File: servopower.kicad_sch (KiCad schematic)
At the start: 18 parts, among them IC1 SIC437DED-T1-GE3

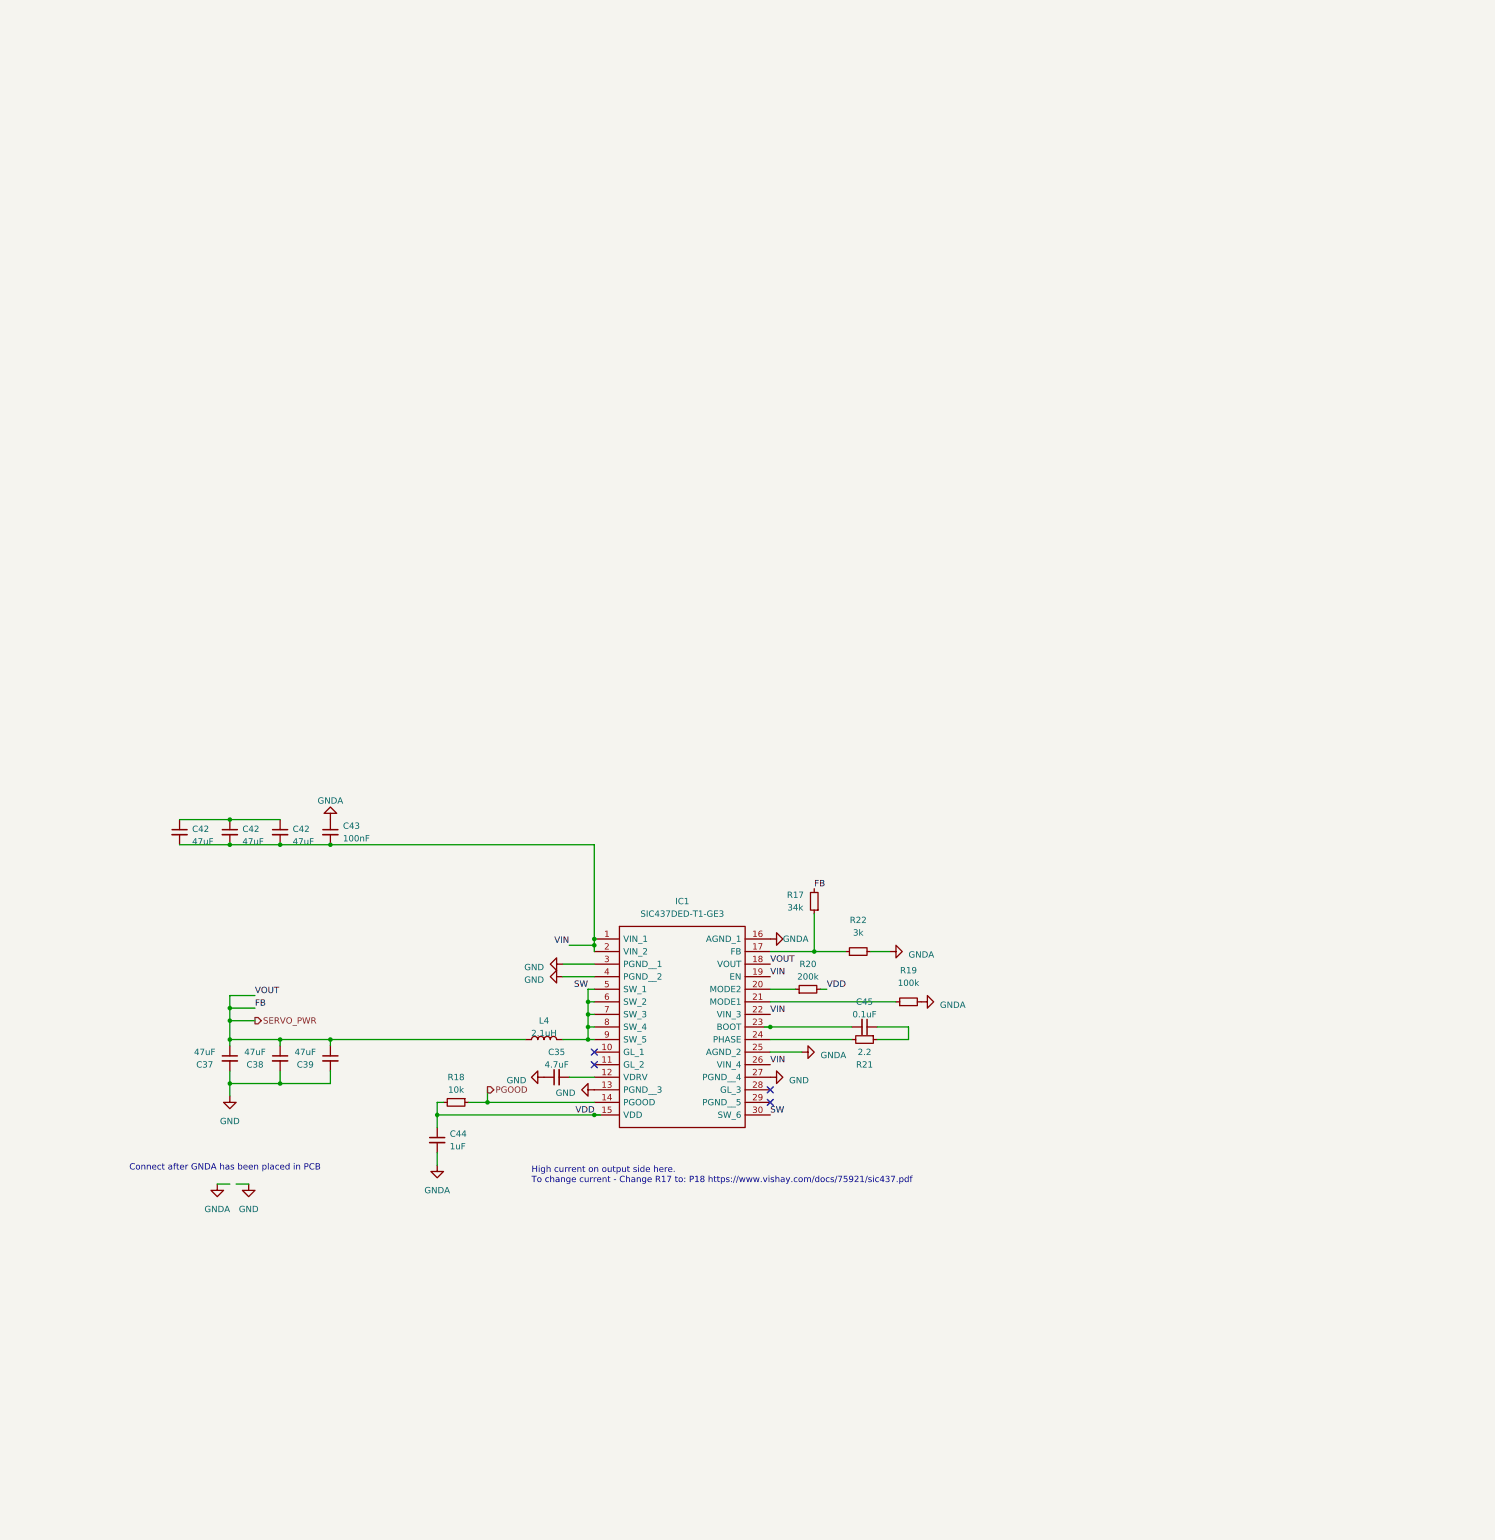
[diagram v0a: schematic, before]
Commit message: error encountered - battery logic and inductor
- use large capacitor?
- use VBUS as a power source?
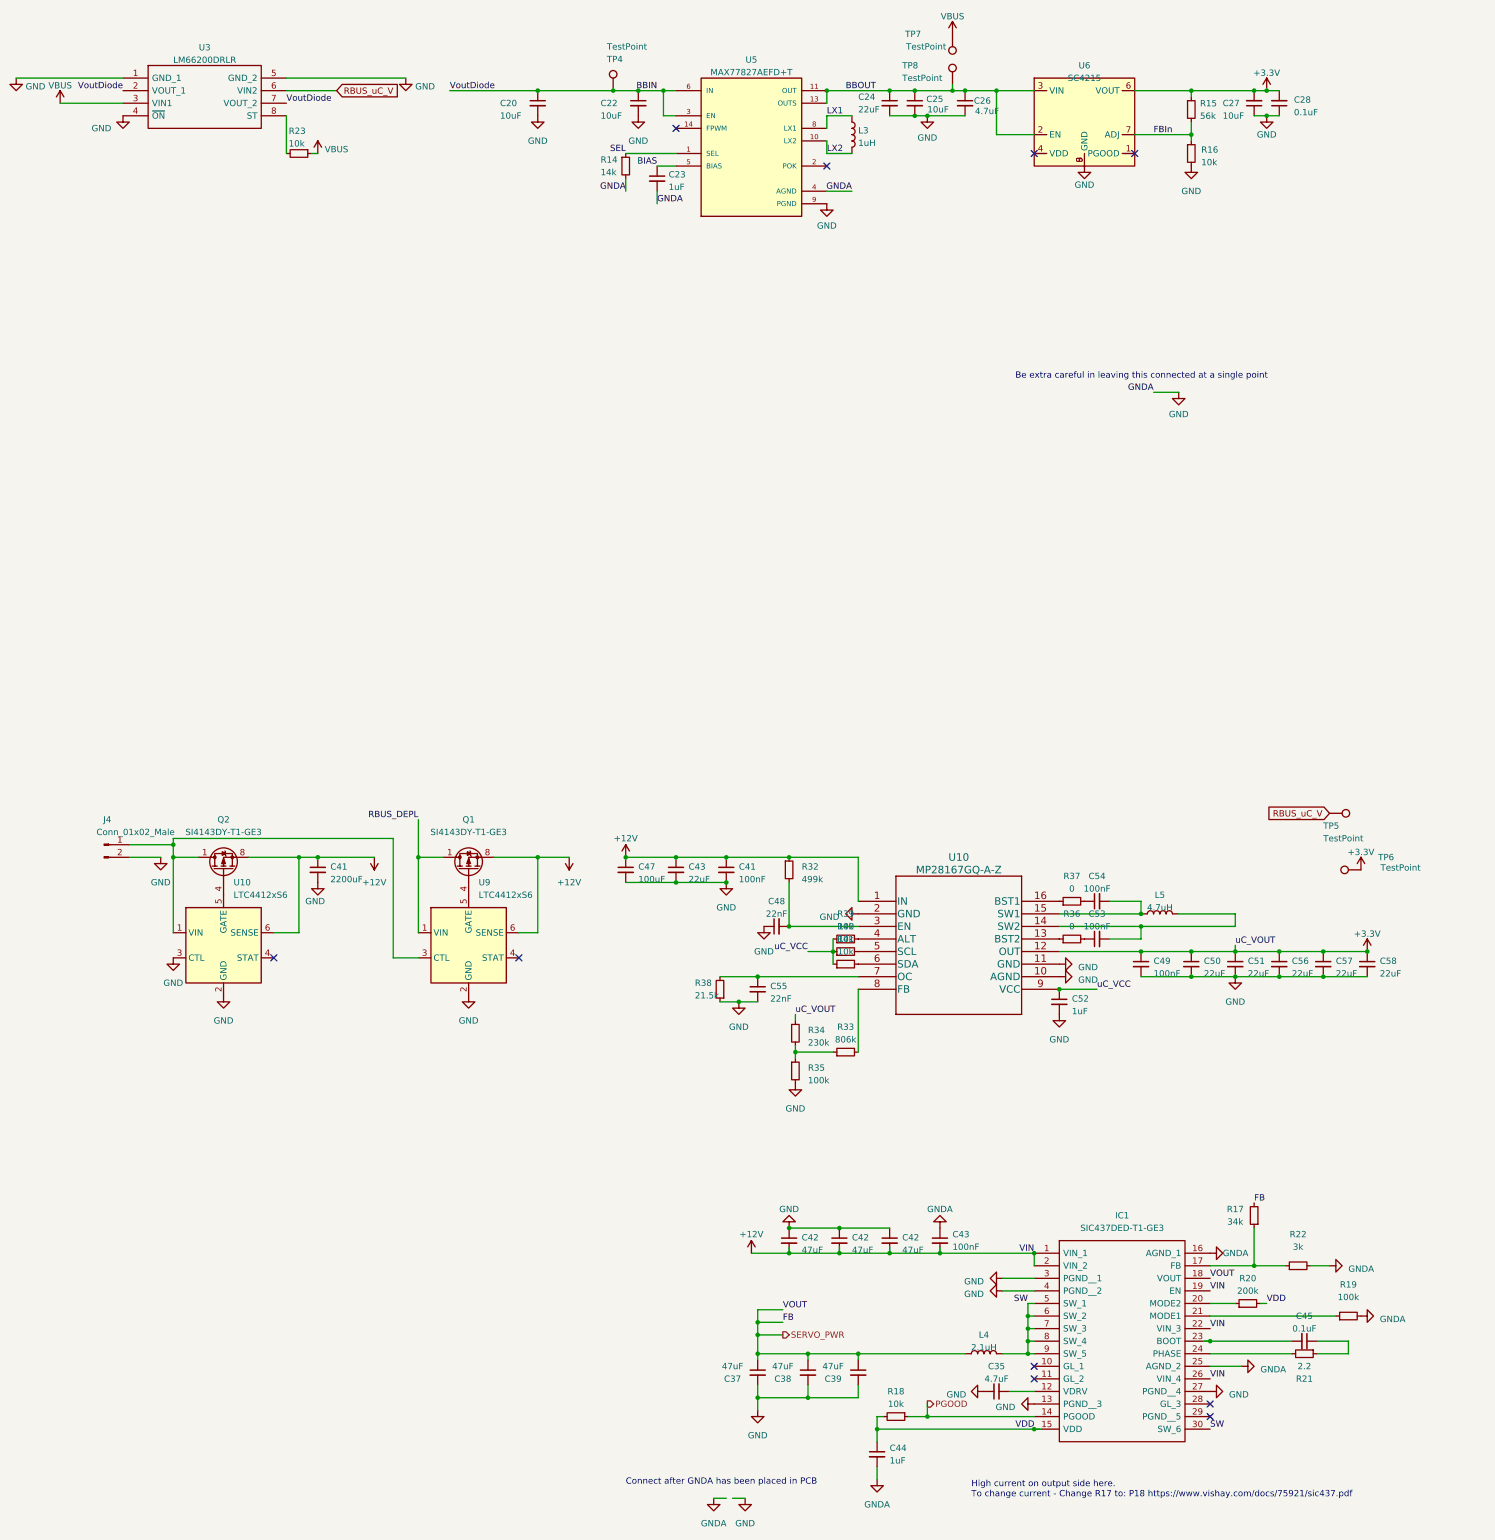
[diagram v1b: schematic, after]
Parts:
- added C20, C25, C27: 10uF, Capacitor_SMD:C_0402_1005Metric, symbol Device:C_Small
- added C22: 10uF, Capacitor_SMD:C_0603_1608Metric, symbol Device:C_Small
- added C23: 1uF, Capacitor_SMD:C_0402_1005Metric, symbol Device:C_Small
- added C24: 22uF, Capacitor_SMD:C_0603_1608Metric, symbol Device:C_Small
- added C26: 4.7uF, Capacitor_SMD:C_0402_1005Metric, symbol Device:C_Small
- added C28: 0.1uF, Capacitor_SMD:C_0402_1005Metric, symbol Device:C_Small
- added C41, C49, C53, C54: 100nF, symbol Device:C_Small
- added C41: 2200uF, Capacitor_SMD:CP_Elec_16x17.5, symbol Device:C_Small
- added C43, C50, C51, C56, C57, C58: 22uF, symbol Device:C_Small
- added C47: 100uF, symbol Device:C_Small
- added C48, C55: 22nF, symbol Device:C_Small
- added C52: 1uF, symbol Device:C_Small
- added J4: Conn_01x02_Male, iclr:AMASS_XT60PW-F, symbol Connector:Conn_01x02_Male
- added L3: 1uH, Inductor_SMD:L_0805_2012Metric, symbol Device:L
- added L5: 4.7uH, symbol Device:L
- added Q1, Q2: SI4143DY-T1-GE3, Package_SO:SOIC-8_3.9x4.9mm_P1.27mm, symbol Device:Q_PMOS_GDS
- added R14: 14k, Resistor_SMD:R_0402_1005Metric, symbol Device:R_Small
- added R15: 56k, Resistor_SMD:R_0402_1005Metric, symbol Device:R_Small
- added R16, R23: 10k, Resistor_SMD:R_0402_1005Metric, symbol Device:R_Small
- added R32: 499k, symbol Device:R_Small
- added R33: 806k, symbol Device:R_Small
- added R34: 230k, symbol Device:R_Small
- added R35: 100k, symbol Device:R_Small
- added R36, R37: 0, symbol Device:R_Small
- added R38: 21.5k, symbol Device:R_Small
- added R39, R40, R41: 10k, symbol Device:R_Small
- added TP4, TP5, TP6, TP7, TP8: TestPoint, TestPoint:TestPoint_Pad_D1.5mm, symbol Connector:TestPoint
- added U10, U9: LTC4412xS6, Package_TO_SOT_SMD:TSOT-23-6, symbol Power_Management:LTC4412xS6
- added U10: MP28167GQ-A-Z, QFN-16_MP28167_MNP, symbol iclr:MP28167GQ-A-Z
- added U3: LM66200DRLR, iclr:SOTFL50P160X60-8N, symbol iclr:LM66200DRLR
- added U5: MAX77827AEFD+T, iclr:CONV_MAX77827AEFD+T, symbol iclr:MAX77827AEFD+T
- added U6: SC4215, iclr:SOIC127P599X175-9N, symbol iclr:RT9025-25GSP
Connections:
- net GNDA is gone; now on net GND: C43.1, C44.2, IC1.16 (AGND_1), IC1.25 (AGND_2), R19.2, R22.2
- net GND: now also C42.1, C42.1, C42.1, C20.2, C22.2, C23.2, C24.2, C25.2, C26.2, C27.1, C28.1, C41.2, C41.2, C43.2, C47.2, C48.1, C49.2, C50.2, C51.2, C52.2, C55.2, C56.2, C57.2, C58.2, J4.2 (Pin_2), R14.2, R16.2, R35.2, R38.1, U10.10 (AGND), U10.11 (GND), U10.2 (GND), U10.2 (GND), U10.3 (CTL), U3.1 (GND_1), U3.4 (~{ON}), U3.5 (GND_2), U5.4 (AGND), U5.9 (PGND), U6.8 (GND), U6.9 (GND), U9.2 (GND)
- net VIN renamed +12V
- net +12V: now also C41.1, C41.1, C43.1, C47.1, Q1.5 (D), Q1.6 (D), Q1.7 (D), Q1.8 (D), Q2.5 (D), Q2.6 (D), Q2.7 (D), Q2.8 (D), R32.1, U10.1 (IN), U10.6 (SENSE), U9.6 (SENSE)
- new net: C53.1, R36.2
- new net: C53.2, L5.2, U10.14 (SW2)
- new net: J4.1 (Pin_1), Q2.1 (S), Q2.2 (S), Q2.3 (S), U10.1 (VIN), U9.3 (CTL)
- new net: Q2.4 (G), U10.5 (GATE)
- new net: C54.1, R37.2
- new net: C54.2, L5.1, U10.15 (SW1)
- new net: Q1.4 (G), U9.5 (GATE)
- new net: C48.2, R32.2, U10.3 (EN)
- new net: R33.1, R34.2, R35.1
- new net: R33.2, U10.8 (FB)
- new net: R40.2, U10.5 (SCL)
- new net: R36.1, U10.13 (BST2)
- new net: C55.1, R38.2, U10.7 (OC)
- new net: R37.1, U10.16 (BST1)
- new net: R23.2, U3.8 (ST)
- new net: R41.2, U10.6 (SDA)
- new net: R39.2, U10.4 (ALT)
- new net +3V3: C27.2, C28.2, C49.1, C50.1, C51.1, C56.1, C57.1, C58.1, R15.1, R34.1, TP6.1, U10.12 (OUT), U6.6 (VOUT)
- new net BBIN: C20.1, C22.1, TP4.1, U3.2 (VOUT_1), U3.7 (VOUT_2), U5.3 (EN), U5.6 (IN)
- new net BBOUT: C24.1, C25.1, C26.1, TP8.1, U5.11 (OUT), U5.13 (OUTS), U6.2 (EN), U6.3 (VIN)
- new net BIAS: C23.1, U5.5 (BIAS)
- new net FBIn: R15.2, R16.1, U6.7 (ADJ)
- new net LX1: L3.1, U5.8 (LX1)
- new net LX2: L3.2, U5.10 (LX2)
- new net RBUS_DEPL: Q1.1 (S), Q1.2 (S), Q1.3 (S), U9.1 (VIN)
- new net RBUS_uC_V: TP5.1, U3.6 (VIN2)
- new net SEL: R14.1, U5.1 (SEL)
- new net VBUS: R23.1, TP7.1, U3.3 (VIN1)
- new net uC_VCC: C52.1, R39.1, R40.1, R41.1, U10.9 (VCC)
- no-connect marks 4 -> 10
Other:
- note added: "Be extra careful in leaving this connected at a single point"
- moved on the sheet: C35, C37, C38, C39, C42, C43, C44, C45, IC1, L4, R17, R18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

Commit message: power draft 2, power fixed I think
10 mosfets now!

2 each on:

Servo power: 3s/4s LIPO, RBUS_DEPL
3.3: VBUS, RBUS_3.3, 3s/4s LIPO

fixed some capacitors
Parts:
- removed C20, C25, C27: 10uF, Capacitor_SMD:C_0402_1005Metric, symbol Device:C_Small
- removed C22: 10uF, Capacitor_SMD:C_0603_1608Metric, symbol Device:C_Small
- removed C23: 1uF, Capacitor_SMD:C_0402_1005Metric, symbol Device:C_Small
- removed C24: 22uF, Capacitor_SMD:C_0603_1608Metric, symbol Device:C_Small
- removed C26: 4.7uF, Capacitor_SMD:C_0402_1005Metric, symbol Device:C_Small
- removed C28: 0.1uF, Capacitor_SMD:C_0402_1005Metric, symbol Device:C_Small
- removed C41: 2200uF, Capacitor_SMD:CP_Elec_16x17.5, symbol Device:C_Small
- removed J4: Conn_01x02_Male, iclr:AMASS_XT60PW-F, symbol Connector:Conn_01x02_Male
- removed L3: 1uH, Inductor_SMD:L_0805_2012Metric, symbol Device:L
- removed Q1, Q2: SI4143DY-T1-GE3, Package_SO:SOIC-8_3.9x4.9mm_P1.27mm, symbol Device:Q_PMOS_GDS
- removed R14: 14k, Resistor_SMD:R_0402_1005Metric, symbol Device:R_Small
- removed R15: 56k, Resistor_SMD:R_0402_1005Metric, symbol Device:R_Small
- removed R16, R23: 10k, Resistor_SMD:R_0402_1005Metric, symbol Device:R_Small
- removed TP4, TP5, TP7, TP8: TestPoint, TestPoint:TestPoint_Pad_D1.5mm, symbol Connector:TestPoint
- removed U10, U9: LTC4412xS6, Package_TO_SOT_SMD:TSOT-23-6, symbol Power_Management:LTC4412xS6
- removed U3: LM66200DRLR, iclr:SOTFL50P160X60-8N, symbol iclr:LM66200DRLR
- removed U5: MAX77827AEFD+T, iclr:CONV_MAX77827AEFD+T, symbol iclr:MAX77827AEFD+T
- removed U6: SC4215, iclr:SOIC127P599X175-9N, symbol iclr:RT9025-25GSP
- C41, C48, C49, C52, C53, C54: footprint (none) -> Capacitor_SMD:C_0402_1005Metric
- C43, C50, C51, C55, C56, C57, C58: footprint (none) -> Capacitor_SMD:C_0805_2012Metric
- C47: footprint (none) -> Capacitor_SMD:CP_Elec_6.3x5.4
- L5: footprint (none) -> iclr:MPLAL60504R7
- R32, R33, R34, R35, R38, R39, R40, R41: footprint (none) -> Resistor_SMD:R_0402_1005Metric
- R36, R37: footprint (none) -> Resistor_SMD:R_0603_1608Metric
- U10: footprint QFN-16_MP28167_MNP -> iclr:MP28167GQ-A-Z
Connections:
- net +12V: no longer C41.1, C43.1, C47.1, R32.1, U10.1 (IN)
- net GND: no longer C43.1, C44.2, IC1.16 (AGND_1), IC1.25 (AGND_2), R19.2, R22.2
- net RBUS_uC_V: now also C41.1, C43.1, C47.1, R32.1, U10.1 (IN)
- new net GNDA: C43.1, C44.2, IC1.16 (AGND_1), IC1.25 (AGND_2), R19.2, R22.2
- no-connect marks 10 -> 4
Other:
- note removed: "Be extra careful in leaving this connected at a single point"

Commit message: PCB layout work
pcb layout work
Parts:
- renumbered TP6 to TP4
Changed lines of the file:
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@@
   (symbol (lib_id "power:+3.3V") (at 273.05 50.8 0) (unit 1)
     (in_bom yes) (on_board yes) (dnp no) (fields_autoplaced)
-    (property "Reference" "#PWR052" (at 273.05 54.61 0)
+    (property "Reference" "#PWR096" (at 273.05 54.61 0)
       (effects (font (size 1.27 1.27)) hide)
     )
@@
   (symbol (lib_id "power:+3.3V") (at 271.78 34.29 0) (unit 1)
     (in_bom yes) (on_board yes) (dnp no) (fields_autoplaced)
-    (property "Reference" "#PWR045" (at 271.78 38.1 0)
+    (property "Reference" "#PWR046" (at 271.78 38.1 0)
       (effects (font (size 1.27 1.27)) hide)
     )
@@
   (symbol (lib_id "Connector:TestPoint") (at 271.78 34.29 90) (unit 1)
     (in_bom yes) (on_board yes) (dnp no)
-    (property "Reference" "TP6" (at 276.86 31.75 90)
-      (effects (font (size 1.27 1.27)))
-    )
+    (property "Reference" "TP4" (at 276.86 31.75 90)
+      (effects (font (size 1.27 1.27)))
+    )

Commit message: schematic review updated
fixed:
-pin 1 on the bootjumper is missing a connection. 
- Move the SD card to a 2nd SPI bus (so a 2nd set of MISO, MOSI, SCLK) as the rest of the bus is blocked while data is written to it, which would interrupt sensor readings. 
- Add a pull-up resistor on the DET_A pin of the micro SD card, and also connect that pin to the esp32 (picture from pickle) 
- VDD on the IMU (U7) is not connected to any power, should be connected to 3.3V 
- Turns out CAN capacitors C18, C19 actually aren’t needed. It’s up to you if you want to keep them, but if you do keep them could you change their value to “DNP” (stands for Do not place) 
-  Add test points to lines which can potentially cause issues. Most of the time this just means places that are connected to the ESP32, but especially places like the SPI lines (including chip selects). Also, add test points to TXD and RXD on the esp32 in case we have to solder to them for programming  

Servo Buck Converter 
- Pin 29 missing ground connection 
-  Add a text label with the part number of the 2.1uH inductor 

LTC4412s 
- No power net connected to Vin 
- stocky diodes replaced logic mosfets
- switched mosfets around so S is common
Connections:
- net GND: now also IC1.29 (PGND__5)
- no-connect marks 4 -> 3
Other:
- note added: "WLPMA0A040M2R2LC"
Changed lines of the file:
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@@
   (no_connect (at 241.3 142.24))
   (no_connect (at 205.74 137.16))
-  (no_connect (at 241.3 144.78))
   (no_connect (at 205.74 134.62))
   (wire (pts (xy 241.3 124.46) (xy 266.7 124.46))
@@
     (stroke (width 0) (type default))
   )
+  (wire (pts (xy 241.3 144.78) (xy 247.65 144.78))
+    (stroke (width 0) (type default))
+  )
   (wire (pts (xy 210.82 43.18) (xy 227.33 43.18))
     (stroke (width 0) (type default))
   )
   (wire (pts (xy 247.65 134.62) (xy 241.3 134.62))
+    (stroke (width 0) (type default))
+  )
+  (wire (pts (xy 247.65 139.7) (xy 241.3 139.7))
     (stroke (width 0) (type default))
   )
@@
     (at 193.04 161.29 0)
     (effects (font (size 1.27 1.27)) (justify left bottom))
+  )
+  (text "WLPMA0A040M2R2LC" (at 193.04 128.27 0)
+    (effects (font (size 1.27 1.27)) (justify right bottom))
   )
   (label "FB" (at 154.94 125.73 0) (fields_autoplaced)
@@
     )
   )
-  (symbol (lib_id "power:GND") (at 241.3 139.7 90) (unit 1)
-    (in_bom yes) (on_board yes) (dnp no) (fields_autoplaced)
-    (property "Reference" "#PWR077" (at 247.65 139.7 0)
-      (effects (font (size 1.27 1.27)) hide)
-    )
-    (property "Value" "GND" (at 245.11 140.335 90)
-      (effects (font (size 1.27 1.27)) (justify right))
-    )
-    (property "Footprint" "" (at 241.3 139.7 0)
-      (effects (font (size 1.27 1.27)) hide)
-    )
-    (property "Datasheet" "" (at 241.3 139.7 0)
+  (symbol (lib_id "power:GND") (at 247.65 139.7 0) (unit 1)
+    (in_bom yes) (on_board yes) (dnp no) (fields_autoplaced)
+    (property "Reference" "#PWR077" (at 247.65 146.05 0)
+      (effects (font (size 1.27 1.27)) hide)
+    )
+    (property "Value" "GND" (at 250.19 141.605 0)
+      (effects (font (size 1.27 1.27)) (justify left))
+    )
+    (property "Footprint" "" (at 247.65 139.7 0)
+      (effects (font (size 1.27 1.27)) hide)
+    )
+    (property "Datasheet" "" (at 247.65 139.7 0)
       (effects (font (size 1.27 1.27)) hide)
     )
@@
         )
       )
+    )
+  )
+  (symbol (lib_id "power:GND") (at 247.65 144.78 0) (unit 1)
+    (in_bom yes) (on_board yes) (dnp no) (fields_autoplaced)
+    (property "Reference" "#PWR077" (at 247.65 151.13 0)
+      (effects (font (size 1.27 1.27)) hide)
+    )
+    (property "Value" "GND" (at 250.19 146.685 0)
+      (effects (font (size 1.27 1.27)) (justify left))
+    )
+    (property "Footprint" "" (at 247.65 144.78 0)
+      (effects (font (size 1.27 1.27)) hide)
+    )
+    (property "Datasheet" "" (at 247.65 144.78 0)
+      (effects (font (size 1.27 1.27)) hide)
+    )
+    (pin "1")
+    (instances
+      (project "Canardboard"
+        (path "/7db990e4-92e1-4f99-b4d2-435bbec1ba83/e0402675-af14-46ad-ab53-2a6080ba54c9"
+          (reference "#PWR077") (unit 1)
+        )
+        (path "/7db990e4-92e1-4f99-b4d2-435bbec1ba83/9ac1c7a8-1287-4655-8906-f7f2eef1324f"
+          (reference "#PWR028") (unit 1)
+        )
+      )
